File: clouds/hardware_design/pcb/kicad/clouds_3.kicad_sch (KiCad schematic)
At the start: 71 parts

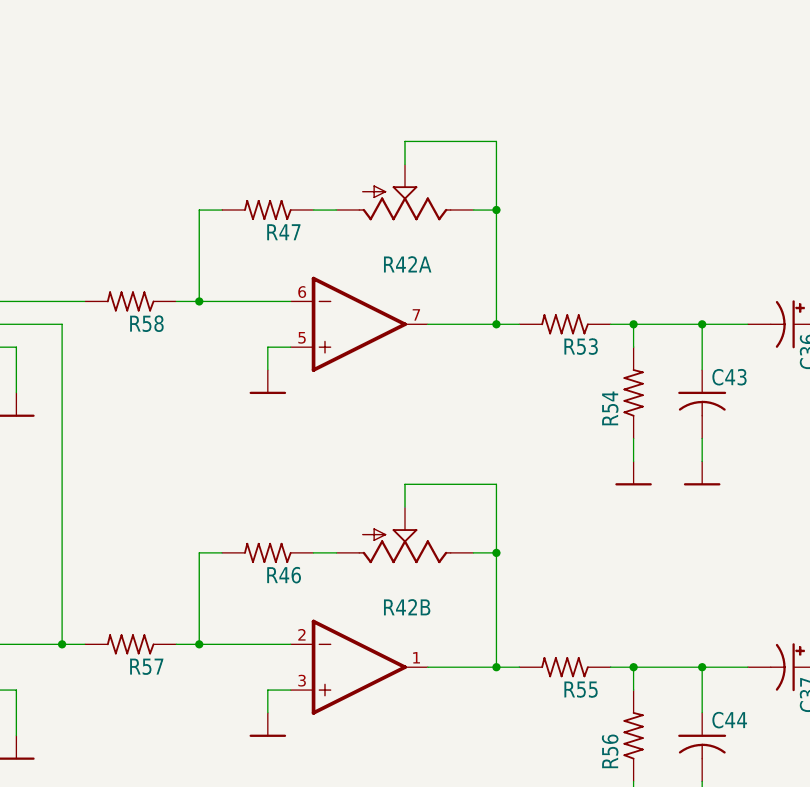
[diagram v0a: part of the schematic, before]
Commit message: clouds: thonk/alpha dual gang pot
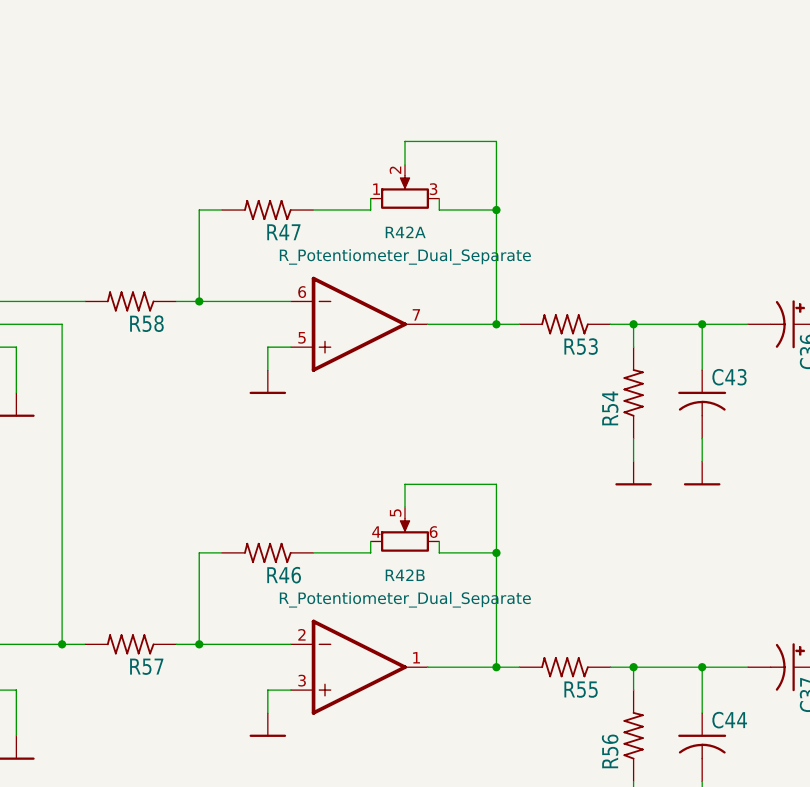
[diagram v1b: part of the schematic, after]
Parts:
- removed R42: (no value), symbol clouds-eagle-import:POT_US_DUAL_GANG
- added R42: R_Potentiometer_Dual_Separate, Potentiometer_THT:Potentiometer_Alpha_RD902F-40-00D_Dual_Vertical_CircularHoles, symbol Device:R_Potentiometer_Dual_Separate
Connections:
- net at IC9.7 (OUT), R53.2: now also R42.2, R42.3
- net at R46.1: now also R42.4
- net at IC9.1 (OUT), R55.2: now also R42.5, R42.6
- net at R47.1: now also R42.1
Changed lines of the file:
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@@
     (stroke (width 0) (type default) (color 0 0 0 0))
   )
-  (wire (pts (xy 149.86 48.26) (xy 147.32 48.26))
+  (wire (pts (xy 143.51 48.26) (xy 149.86 48.26))
     (stroke (width 0) (type default) (color 0 0 0 0))
   )
@@
     (stroke (width 0) (type default) (color 0 0 0 0))
   )
+  (wire (pts (xy 143.51 86.36) (xy 143.51 85.09))
+    (stroke (width 0) (type default) (color 0 0 0 0))
+  )
   (wire (pts (xy 274.32 106.68) (xy 271.78 106.68))
     (stroke (width 0) (type default) (color 0 0 0 0))
@@
     (stroke (width 0) (type default) (color 0 0 0 0))
   )
+  (wire (pts (xy 143.51 48.26) (xy 143.51 46.99))
+    (stroke (width 0) (type default) (color 0 0 0 0))
+  )
   (wire (pts (xy 96.52 228.6) (xy 99.06 228.6))
     (stroke (width 0) (type default) (color 0 0 0 0))
@@
     (stroke (width 0) (type default) (color 0 0 0 0))
   )
+  (wire (pts (xy 135.89 86.36) (xy 135.89 85.09))
+    (stroke (width 0) (type default) (color 0 0 0 0))
+  )
   (wire (pts (xy 241.3 162.56) (xy 241.3 165.1))
     (stroke (width 0) (type default) (color 0 0 0 0))
@@
     (stroke (width 0) (type default) (color 0 0 0 0))
   )
-  (wire (pts (xy 129.54 86.36) (xy 132.08 86.36))
-    (stroke (width 0) (type default) (color 0 0 0 0))
-  )
   (wire (pts (xy 238.76 104.14) (xy 236.22 104.14))
     (stroke (width 0) (type default) (color 0 0 0 0))
@@
     (stroke (width 0) (type default) (color 0 0 0 0))
   )
-  (wire (pts (xy 129.54 48.26) (xy 132.08 48.26))
+  (wire (pts (xy 129.54 48.26) (xy 135.89 48.26))
     (stroke (width 0) (type default) (color 0 0 0 0))
   )
@@
     (stroke (width 0) (type default) (color 0 0 0 0))
   )
+  (wire (pts (xy 135.89 48.26) (xy 135.89 46.99))
+    (stroke (width 0) (type default) (color 0 0 0 0))
+  )
   (wire (pts (xy 314.96 86.36) (xy 314.96 91.44))
     (stroke (width 0) (type default) (color 0 0 0 0))
@@
     (stroke (width 0) (type default) (color 0 0 0 0))
   )
-  (wire (pts (xy 149.86 86.36) (xy 147.32 86.36))
+  (wire (pts (xy 143.51 86.36) (xy 149.86 86.36))
     (stroke (width 0) (type default) (color 0 0 0 0))
   )
@@
   )
   (wire (pts (xy 96.52 218.44) (xy 96.52 220.98))
+    (stroke (width 0) (type default) (color 0 0 0 0))
+  )
+  (wire (pts (xy 129.54 86.36) (xy 135.89 86.36))
     (stroke (width 0) (type default) (color 0 0 0 0))
   )
@@
     (pin "2")
   )
+  (symbol (lib_id "Device:R_Potentiometer_Dual_Separate") (at 139.7 85.09 90) (unit 2)
+    (in_bom yes) (on_board yes) (fields_autoplaced)
+    (property "Reference" "R42" (id 0) (at 139.7 88.9 90))
+    (property "Value" "R_Potentiometer_Dual_Separate" (id 1) (at 139.7 91.44 90))
+    (property "Footprint" "Potentiometer_THT:Potentiometer_Alpha_RD902F-40-00D_Dual_Vertical_CircularHoles" (id 2) (at 139.7 85.09 0)
+      (effects (font (size 1.27 1.27)) hide)
+    )
+    (property "Datasheet" "~" (id 3) (at 139.7 85.09 0)
+      (effects (font (size 1.27 1.27)) hide)
+    )
+    (pin "1")
+    (pin "2")
+    (pin "3")
+    (pin "4")
+    (pin "5")
+    (pin "6")
+  )
   (symbol (lib_id "clouds-eagle-import:C-USC0603") (at 330.2 83.82 0) (unit 1)
     (in_bom yes) (on_board yes)
@@
     (pin "1")
     (pin "2")
-  )
-  (symbol (lib_id "clouds-eagle-import:POT_US_DUAL_GANG") (at 139.7 86.36 270) (mirror x) (unit 2)
-    (in_bom yes) (on_board yes)
-    (property "Reference" "R42" (id 0) (at 137.16 91.44 90)
-      (effects (font (size 1.778 1.5113)) (justify left bottom))
-    )
-    (property "Value" "" (id 1) (at 137.16 88.9 90)
-      (effects (font (size 1.778 1.5113)) (justify left bottom))
-    )
-    (property "Footprint" "" (id 2) (at 139.7 86.36 0)
-      (effects (font (size 1.27 1.27)) hide)
-    )
-    (property "Datasheet" "" (id 3) (at 139.7 86.36 0)
-      (effects (font (size 1.27 1.27)) hide)
-    )
-    (pin "1P")
-    (pin "2P")
-    (pin "3P")
-    (pin "1")
-    (pin "2")
-    (pin "3")
   )
   (symbol (lib_id "clouds-eagle-import:GND") (at 236.22 109.22 0) (unit 1)
@@
       (effects (font (size 1.27 1.27)) hide)
     )
-    (property "Value" "" (id 1) (at 17.78 279.4 0)
-      (effects (font (size 1.27 1.27)) hide)
-    )
-    (property "Footprint" "" (id 2) (at 17.78 279.4 0)
+    (property "Value" "A3L-LOC" (id 1) (at 17.78 279.4 0)
+      (effects (font (size 1.27 1.27)) hide)
+    )
+    (property "Footprint" "clouds:" (id 2) (at 17.78 279.4 0)
       (effects (font (size 1.27 1.27)) hide)
     )
@@
     (pin "2")
   )
-  (symbol (lib_id "clouds-eagle-import:POT_US_DUAL_GANG") (at 139.7 48.26 270) (mirror x) (unit 1)
-    (in_bom yes) (on_board yes)
-    (property "Reference" "R42" (id 0) (at 137.16 53.34 90)
-      (effects (font (size 1.778 1.5113)) (justify left bottom))
-    )
-    (property "Value" "" (id 1) (at 137.16 50.8 90)
-      (effects (font (size 1.778 1.5113)) (justify left bottom))
-    )
-    (property "Footprint" "" (id 2) (at 139.7 48.26 0)
-      (effects (font (size 1.27 1.27)) hide)
-    )
-    (property "Datasheet" "" (id 3) (at 139.7 48.26 0)
-      (effects (font (size 1.27 1.27)) hide)
-    )
-    (pin "1P")
-    (pin "2P")
-    (pin "3P")
-    (pin "1")
-    (pin "2")
-    (pin "3")
-  )
   (symbol (lib_id "clouds-eagle-import:C-USC0603") (at 109.22 157.48 90) (unit 1)
     (in_bom yes) (on_board yes)
@@
     (pin "P3")
   )
+  (symbol (lib_id "Device:R_Potentiometer_Dual_Separate") (at 139.7 46.99 90) (unit 1)
+    (in_bom yes) (on_board yes) (fields_autoplaced)
+    (property "Reference" "R42" (id 0) (at 139.7 50.8 90))
+    (property "Value" "R_Potentiometer_Dual_Separate" (id 1) (at 139.7 53.34 90))
+    (property "Footprint" "Potentiometer_THT:Potentiometer_Alpha_RD902F-40-00D_Dual_Vertical_CircularHoles" (id 2) (at 139.7 46.99 0)
+      (effects (font (size 1.27 1.27)) hide)
+    )
+    (property "Datasheet" "~" (id 3) (at 139.7 46.99 0)
+      (effects (font (size 1.27 1.27)) hide)
+    )
+    (pin "1")
+    (pin "2")
+    (pin "3")
+    (pin "4")
+    (pin "5")
+    (pin "6")
+  )
   (symbol (lib_id "clouds-eagle-import:TL074D") (at 314.96 195.58 0) (unit 5)
